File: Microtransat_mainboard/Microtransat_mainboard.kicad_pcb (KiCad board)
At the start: 2 copper layers, 110 x 110 mm, 49 parts, among them J1 Conn_01x06, J10 Conn_01x04, J101 12V IN, J11 Conn_01x03, J12 Conn_01x03, J13 Conn_01x03, J2 Conn_01x04, J3 Conn_01x07, J301 ESTOP IN, J4 Conn_01x04, J5 Conn_01x02, J6 Conn_01x03, J9 Conn_01x04, K301 12V SRD Form C, SW1 SW_SPDT, U1 GPS 746, U2 SD Card Module 254, U3 IMU 4754

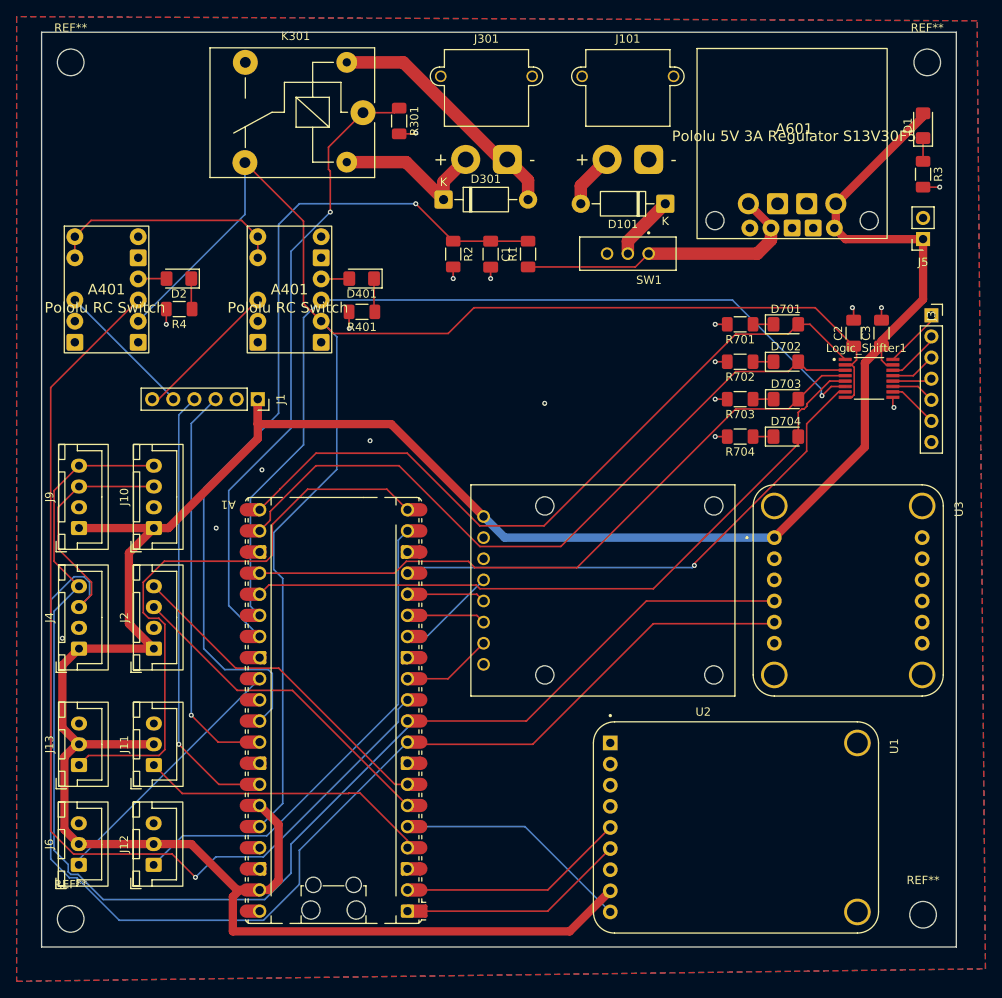
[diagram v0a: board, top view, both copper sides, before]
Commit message: Updated PCB silkscreen
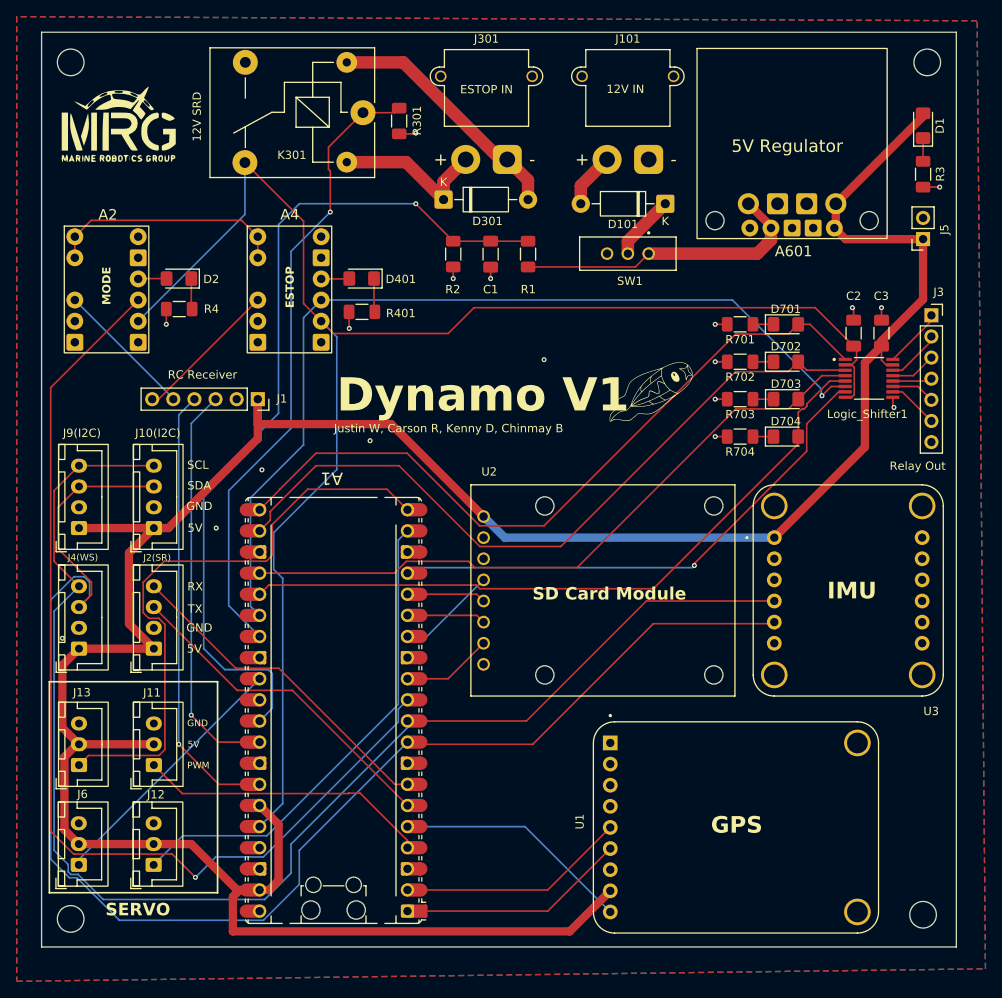
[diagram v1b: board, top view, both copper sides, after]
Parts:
- added G***: LOGO, graphics:MRG, F.Cu at (67.3, 42.8)
- added G***: LOGO, graphics:tynamo, F.Cu at (131.3, 74.2)
- renumbered J10 to J10(I2C), J2 to J2(SR), J4 to J4(WS), J9 to J9(I2C)
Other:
- board text added: "12V IN"
- board text added: "12V SRD"
- board text added: "5V"
- board text added: "5V Regulator"
- board text added: "Dynamo V1"
- board text added: "ESTOP"
- board text added: "ESTOP IN"
- board text added: "GND"
- board text added: "GPS"
- board text added: "IMU"
- board text added: "Justin W, Carson R, Kenny D, Chinmay B"
- board text added: "MODE"
- board text added: "PWM"
- board text added: "RC Receiver"
- board text added: "RX"
- board text added: "Relay Out"
- board text added: "SCL"
- board text added: "SD Card Module"
- board text added: "SDA"
- board text added: "SERVO"
- board text added: "TX"

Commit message: Finished silkscreen/outline changes
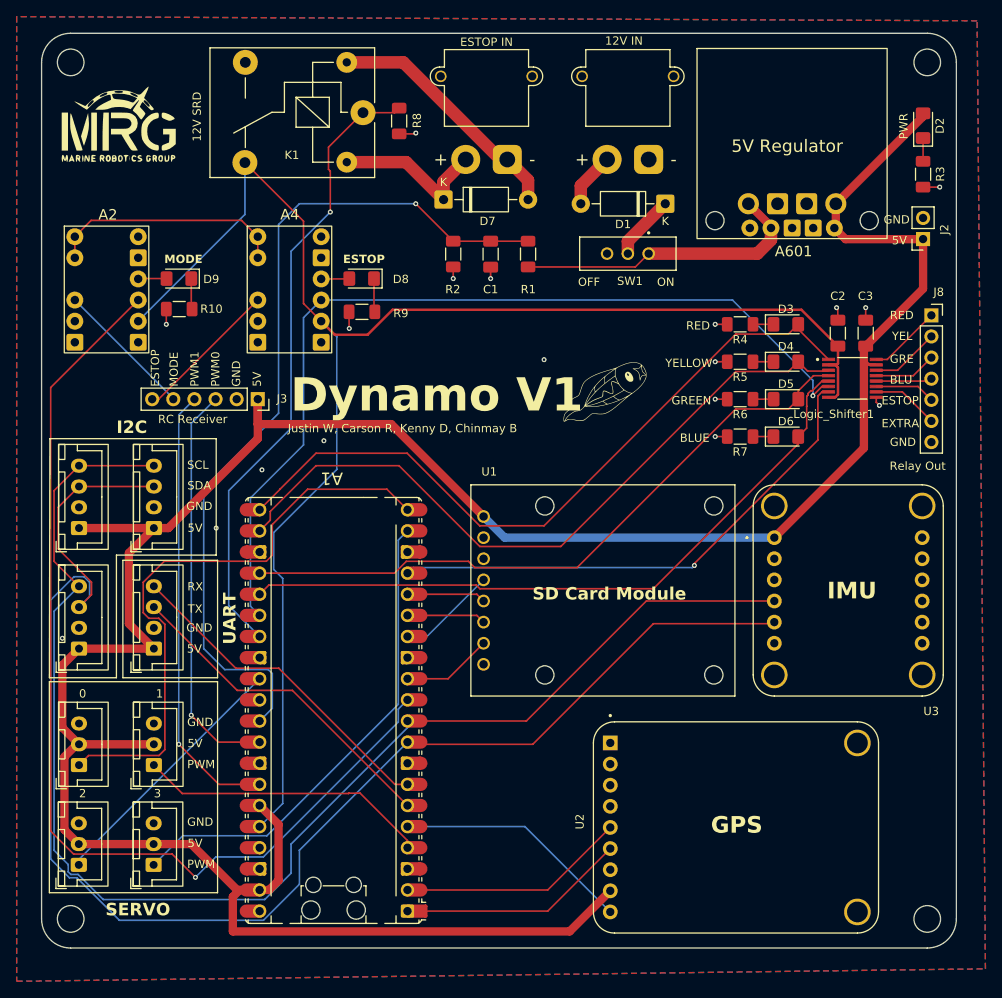
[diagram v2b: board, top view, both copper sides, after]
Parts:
- moved G*** 5.55 mm to (125.8, 74.2)
- moved Logic_Shifter1 2.00 mm to (155.5, 72.5)
- moved C2 1.90 mm to (153.8, 67.1)
- moved C3 1.90 mm to (157.1, 67.1)
- moved REF** 0.71 mm to (164.5, 137.5)
- renumbered A4 to A2, A601 to A3, A2 to A4, D101 to D1, D1 to D2, D701 to D3, D702 to D4, D703 to D5, D704 to D6, D301 to D7, D401 to D8, D2 to D9, J101 to J1, J12 to J10, J13 to J11, J6 to J12, J301 to J13, J5 to J2, J1 to J3, J9(I2C) to J4, J10(I2C) to J5, J4(WS) to J6, J2(SR) to J7, J3 to J8, J11 to J9, K301 to K1, R4 to R10, R701 to R4, R702 to R5, R703 to R6, R704 to R7, R301 to R8, R401 to R9, U2 to U1, U1 to U2
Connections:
- A1 pad 19: /PWM1 -> /PWM3
- A1 pad 20: /PWM2 -> /PWM0
- A1 pad 29: /PWM3 -> /PWM2
- A1 pad 4: /PWM0 -> /PWM1
- J10 pad 1: /PWM1 -> /PWM3
- J11 pad 1: /PWM2 -> /PWM0
- J12 pad 1: /PWM3 -> /PWM2
- J9 pad 1: /PWM0 -> /PWM1
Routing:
- net /PWM2: track 72.6 -> 31.4 mm
- net /PWM0: track 35.2 -> 72.6 mm
- net /PWM3: track 31.4 -> 58.7 mm
- net /PWM1: track 58.7 -> 35.2 mm
- net /Relay Board Interface/greenOut: track 5.53 -> 7.53 mm
- net /Relay Board Interface/eStopOut: track 5.29 -> 7.29 mm
- net /Relay Board Interface/blueOut: track 4.75 -> 6.75 mm
- net /Relay Board Interface/relay0Out: track 6.08 -> 8.08 mm
- net /yellow: track 87.9 -> 86.0 mm
- net /Relay Board Interface/yellowOut: track 6.63 -> 8.31 mm
- net /red: track 88.6 -> 87.0 mm
- net /Relay Board Interface/redOut: track 7.22 -> 8.83 mm
- net /blue: track 83.8 -> 82.2 mm
- net /green: track 80.9 -> 79.5 mm
- net /GPIO20: track 110.6 -> 109.2 mm
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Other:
- outline, holes or cut-outs redrawn
- board text added: "0"
- board text added: "1"
- board text added: "2"
- board text added: "3"
- board text added: "BLU"
- board text added: "BLUE"
- board text added: "EXTRA"
- board text added: "GRE"
- board text added: "GREEN"
- board text added: "I2C"
- board text added: "OFF"
- board text added: "ON"
- board text added: "PWM0"
- board text added: "PWM1"
- board text added: "PWR"
- board text added: "RED"
- board text added: "UART"
- board text added: "YEL"
- board text added: "YELLOW"

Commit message: Some small changes to silkscreen and component numbers
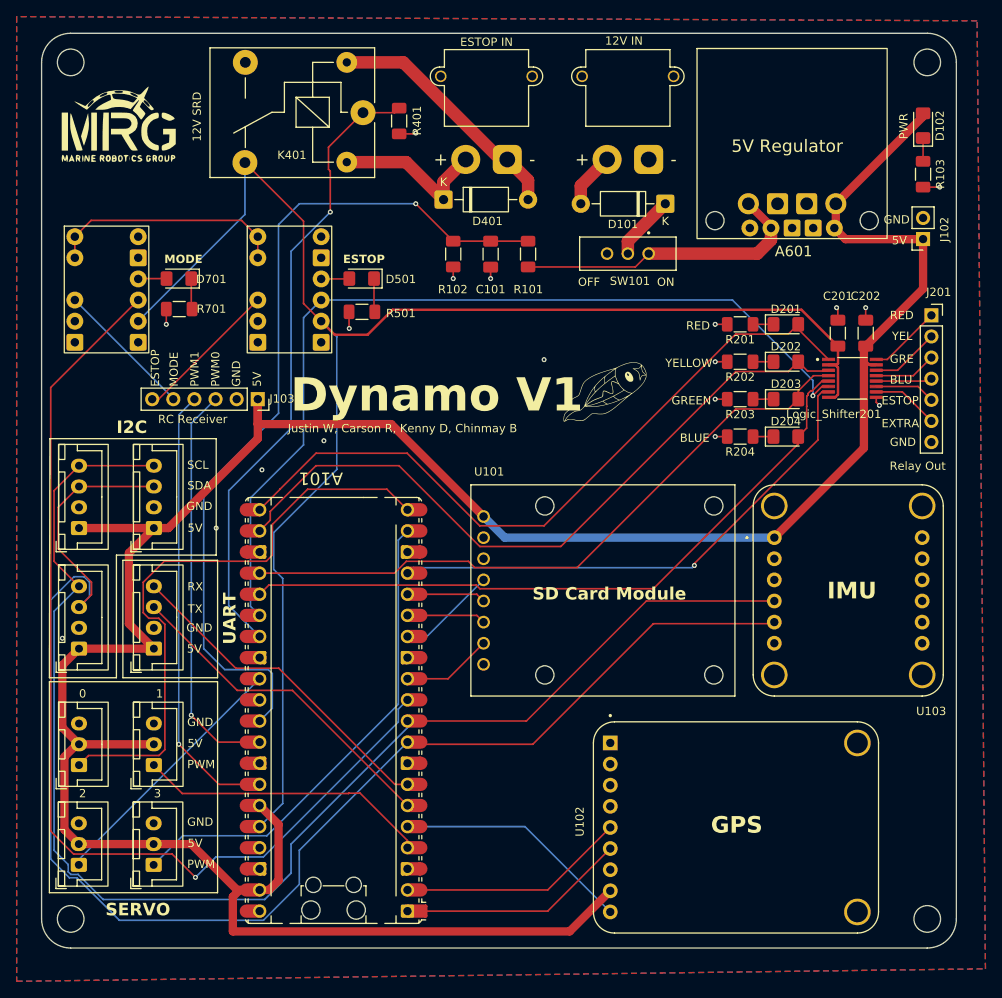
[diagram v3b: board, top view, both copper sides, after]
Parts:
- renumbered A1 to A101, A2 to A501, A3 to A601, A4 to A701, C1 to C101, C2 to C201, C3 to C202, D1 to D101, D2 to D102, D3 to D201, D4 to D202, D5 to D203, D6 to D204, D7 to D401, D8 to D501, D9 to D701, J1 to J101, J2 to J102, J3 to J103, J4 to J104, J5 to J105, J6 to J106, J7 to J107, J8 to J201, J9 to J301, J10 to J302, J11 to J303, J12 to J304, J13 to J401, K1 to K401, Logic_Shifter1 to Logic_Shifter201, R1 to R101, R2 to R102, R3 to R103, R4 to R201, R5 to R202, R6 to R203, R7 to R204, R8 to R401, R9 to R501, R10 to R701, SW1 to SW101, U1 to U101, U2 to U102, U3 to U103

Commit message: Fixed changes from design review
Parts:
- removed A501, A701: ~, Microtransat:Pololu RC Switch
- removed D501, D701: LED, LED_SMD:LED_1206_3216Metric_Pad1.42x1.75mm_HandSolder
- removed J201: Conn_01x07, Connector_PinSocket_2.54mm:PinSocket_1x07_P2.54mm_Vertical
- removed R501, R701: 220, Resistor_SMD:R_1206_3216Metric_Pad1.30x1.75mm_HandSolder
- added D1: LED, LED_SMD:LED_1206_3216Metric_Pad1.42x1.75mm_HandSolder, F.Cu at (149.5, 56.2)
- added D2: LED, LED_SMD:LED_1206_3216Metric_Pad1.42x1.75mm_HandSolder, F.Cu at (149.5, 59.5)
- added J1: Conn_01x06, Connector_JST:JST_XH_B6B-XH-A_1x06_P2.50mm_Vertical, F.Cu at (163.8, 79.0)
- added J2: Conn_01x02, Connector_JST:JST_XH_B2B-XH-A_1x02_P2.50mm_Vertical, F.Cu at (163.8, 63.2)
- added JP1: RC3 to GPIO20, Jumper:SolderJumper-2_P1.3mm_Open_RoundedPad1.0x1.5mm, B.Cu at (83.4, 73.0)
- added JP2: GPIO20 to estop, Jumper:SolderJumper-2_P1.3mm_Open_RoundedPad1.0x1.5mm, B.Cu at (89.7, 76.6)
- added JP3: RC3 to estop, Jumper:SolderJumper-2_P1.3mm_Open_RoundedPad1.0x1.5mm, B.Cu at (83.4, 80.0)
- added R1: 220, Resistor_SMD:R_1206_3216Metric_Pad1.30x1.75mm_HandSolder, F.Cu at (155.3, 56.2)
- added R2: 220, Resistor_SMD:R_1206_3216Metric_Pad1.30x1.75mm_HandSolder, F.Cu at (155.2, 59.5)
- J102: footprint Connector_PinSocket_2.54mm:PinSocket_1x02_P2.54mm_Vertical -> Connector_JST:JST_XH_B2B-XH-A_1x02_P2.50mm_Vertical
- J103: footprint Connector_PinSocket_2.54mm:PinSocket_1x06_P2.54mm_Vertical -> Connector_JST:JST_XH_B6B-XH-A_1x06_P2.50mm_Vertical
- moved G*** 89.0 mm to (114.0, 118.6)
- moved R103 64.3 mm to (103.6, 70.0), turned to 180 degrees
- moved D102 61.3 mm to (109.4, 70.0), turned to 0 degrees
- moved U103 35.0 mm to (120.0, 98.0)
- moved R401 33.8 mm to (76.4, 64.8), turned to 0 degrees
- moved R204 29.7 mm to (155.3, 53.0), turned to 0 degrees
- moved K401 29.2 mm to (75.0, 60.1), turned to 90 degrees
- moved R203 28.5 mm to (155.3, 49.8), turned to 0 degrees
- moved R202 27.4 mm to (155.3, 46.5), turned to 0 degrees
- moved D204 26.6 mm to (149.5, 53.0), turned to 180 degrees
- moved R201 26.4 mm to (155.3, 43.2), turned to 0 degrees
- moved D203 25.3 mm to (149.5, 49.8), turned to 180 degrees
- moved U101 25.0 mm to (150.5, 98.0)
- moved D202 24.1 mm to (149.5, 46.5), turned to 180 degrees
- moved D201 22.8 mm to (149.5, 43.2), turned to 180 degrees
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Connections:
- net /INPWM0 renamed /RC0
- net /INPWM1 renamed /RC1
- A101 pad 11: /MODE -> /RC2
- J103 pad 5: /MODEIN -> /RC2
- J103 pad 6: /eSTOPIN -> /RC3
- Logic_Shifter201 pad 6: /GPIO20 -> /Relay Board Interface/eStopTrigger
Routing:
- net +5V: track 329.5 -> 494.5 mm
- net /MODE: track 123.2 -> 0.00 mm, vias 1 -> 0
- net /RC2: track 0.00 -> 86.2 mm, vias 0 -> 2
- net /Relay Board Interface/eStopTrigger: track 0.00 -> 79.1 mm, vias 0 -> 1
- net /GPIO20: track 109.2 -> 35.8 mm, vias 1 -> 2
- net /VREF: track 103.5 -> 68.1 mm
- net /SDA: track 174.3 -> 143.0 mm
- net /SCL: track 165.1 -> 134.1 mm
- net /SCLK: track 13.5 -> 43.3 mm
- net LOAD_HI: track 28.7 -> 0.00 mm
- net /GPIO21: track 76.0 -> 47.4 mm
- net /CS: track 10.1 -> 35.1 mm
- net /MOSI: track 9.48 -> 34.0 mm
- net /MISO: track 9.48 -> 34.0 mm
- net +3V3: track 188.5 -> 169.7 mm, vias 0 -> 2
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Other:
- board size 110 x 110 mm -> 110 x 101.2 mm
- board text added: "GPIO20 to ESTOP"
- board text added: "RC0"
- board text added: "RC1"
- board text added: "RC2"
- board text added: "RC3"
- board text added: "RC3 to ESTOP"
- board text added: "RC3 to GPIO20"
- board text removed: "MODE"
- board text removed: "PWM0"
- board text removed: "PWM1"
- board text removed: "PWR"

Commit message: Exported production files
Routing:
- net /RC2: track 86.2 -> 51.0 mm, vias 2 -> 1
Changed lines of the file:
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@@
 			(outputformat 1)
 			(mirror no)
-			(drillshape 1)
+			(drillshape 0)
 			(scaleselection 1)
-			(outputdirectory "")
+			(outputdirectory "./fab")
 		)
 	)
@@
 			(pinfunction "A1")
 			(pintype "bidirectional")
-			(solder_mask_margin 0.102)
+			(solder_mask_margin 0)
 		)
 		(pad "2" smd roundrect
@@
 			(pinfunction "VCCA")
 			(pintype "power_in")
-			(solder_mask_margin 0.102)
+			(solder_mask_margin 0)
 		)
 		(pad "3" smd roundrect
@@
 			(pinfunction "A2")
 			(pintype "bidirectional")
-			(solder_mask_margin 0.102)
+			(solder_mask_margin 0)
 		)
 		(pad "4" smd roundrect
@@
 			(pinfunction "A3")
 			(pintype "bidirectional")
-			(solder_mask_margin 0.102)
+			(solder_mask_margin 0)
 		)
 		(pad "5" smd roundrect
@@
 			(pinfunction "A4")
 			(pintype "bidirectional")
-			(solder_mask_margin 0.102)
+			(solder_mask_margin 0)
 		)
 		(pad "6" smd roundrect
@@
 			(pinfunction "A5")
 			(pintype "bidirectional")
-			(solder_mask_margin 0.102)
+			(solder_mask_margin 0)
 		)
 		(pad "7" smd roundrect
@@
 			(pinfunction "A6")
 			(pintype "bidirectional")
-			(solder_mask_margin 0.102)
+			(solder_mask_margin 0)
 		)
 		(pad "8" smd roundrect
@@
 			(pinfunction "OE")
 			(pintype "input")
-			(solder_mask_margin 0.102)
+			(solder_mask_margin 0)
 		)
 		(pad "9" smd roundrect
@@
 			(pinfunction "GND")
 			(pintype "power_in")
-			(solder_mask_margin 0.102)
+			(solder_mask_margin 0)
 		)
 		(pad "10" smd roundrect
@@
 			(pinfunction "B6")
 			(pintype "bidirectional")
-			(solder_mask_margin 0.102)
+			(solder_mask_margin 0)
 		)
 		(pad "11" smd roundrect
@@
 			(pinfunction "B5")
 			(pintype "bidirectional")
-			(solder_mask_margin 0.102)
+			(solder_mask_margin 0)
 		)
 		(pad "12" smd roundrect
@@
 			(pinfunction "B4")
 			(pintype "bidirectional")
-			(solder_mask_margin 0.102)
+			(solder_mask_margin 0)
 		)
 		(pad "13" smd roundrect
@@
 			(pinfunction "B3")
 			(pintype "bidirectional")
-			(solder_mask_margin 0.102)
+			(solder_mask_margin 0)
 		)
 		(pad "14" smd roundrect
@@
 			(pinfunction "B2")
 			(pintype "bidirectional")
-			(solder_mask_margin 0.102)
+			(solder_mask_margin 0)
 		)
 		(pad "15" smd roundrect
@@
 			(pinfunction "VCCB")
 			(pintype "power_in")
-			(solder_mask_margin 0.102)
+			(solder_mask_margin 0)
 		)
 		(pad "16" smd roundrect
@@
 			(pinfunction "B1")
 			(pintype "bidirectional")
-			(solder_mask_margin 0.102)
+			(solder_mask_margin 0)
 		)
 		(embedded_fonts no)
@@
 	)
 	(via
-		(at 76.5 132.5)
-		(size 0.6)
-		(drill 0.3)
-		(layers "F.Cu" "B.Cu")
-		(net 68)
-	)
-	(via
 		(at 99.4 109.6)
 		(size 0.6)
@@
 	)
 	(segment
-		(start 84.67605 130.041)
-		(end 100.899 113.81805)
-		(width 0.2)
-		(layer "B.Cu")
-		(net 68)
-	)
-	(segment
 		(start 85.326 85.826)
 		(end 85.326 95.526)
@@
 	)
 	(segment
-		(start 100.899 113.81805)
-		(end 100.899 112.261)
-		(width 0.2)
-		(layer "B.Cu")
-		(net 68)
-	)
-	(segment
-		(start 100.899 112.261)
-		(end 102 111.16)
-		(width 0.2)
-		(layer "B.Cu")
-		(net 68)
-	)
-	(segment
 		(start 72.5 73)
 		(end 85.326 85.826)
 		(width 0.2)
 		(layer "B.Cu")
-		(net 68)
-	)
-	(segment
-		(start 78.959 130.041)
-		(end 84.67605 130.041)
-		(width 0.2)
-		(layer "B.Cu")
-		(net 68)
-	)
-	(segment
-		(start 76.5 132.5)
-		(end 78.959 130.041)
-		(width 0.2)
-		(layer "B.Cu")
